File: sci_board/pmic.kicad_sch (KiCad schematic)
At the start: 21 parts, among them J1 Conn_01x03_Pin Vertical, U1 STM32L496VGTx

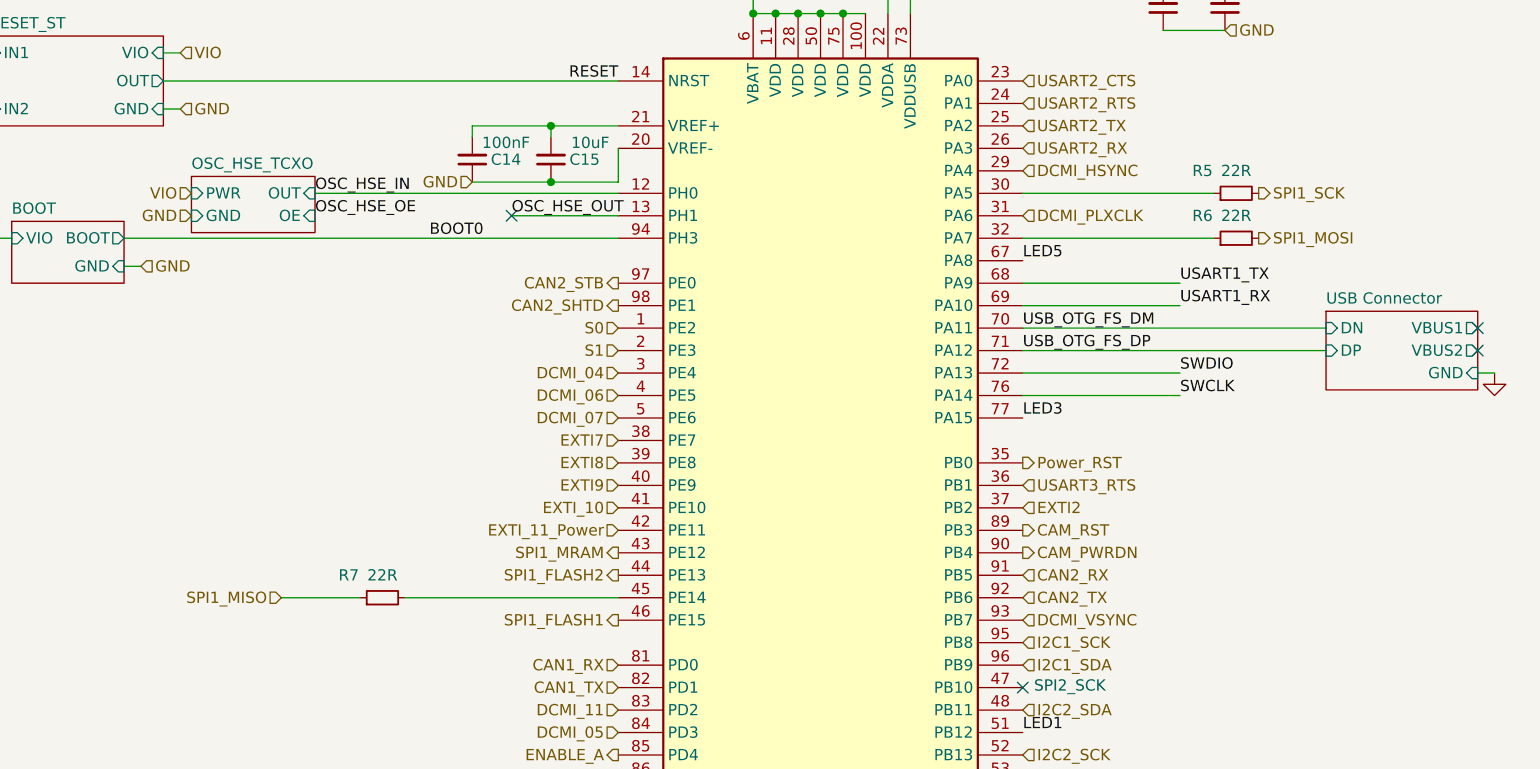
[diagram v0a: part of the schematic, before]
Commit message: SCI AVI and EPS are now consistent
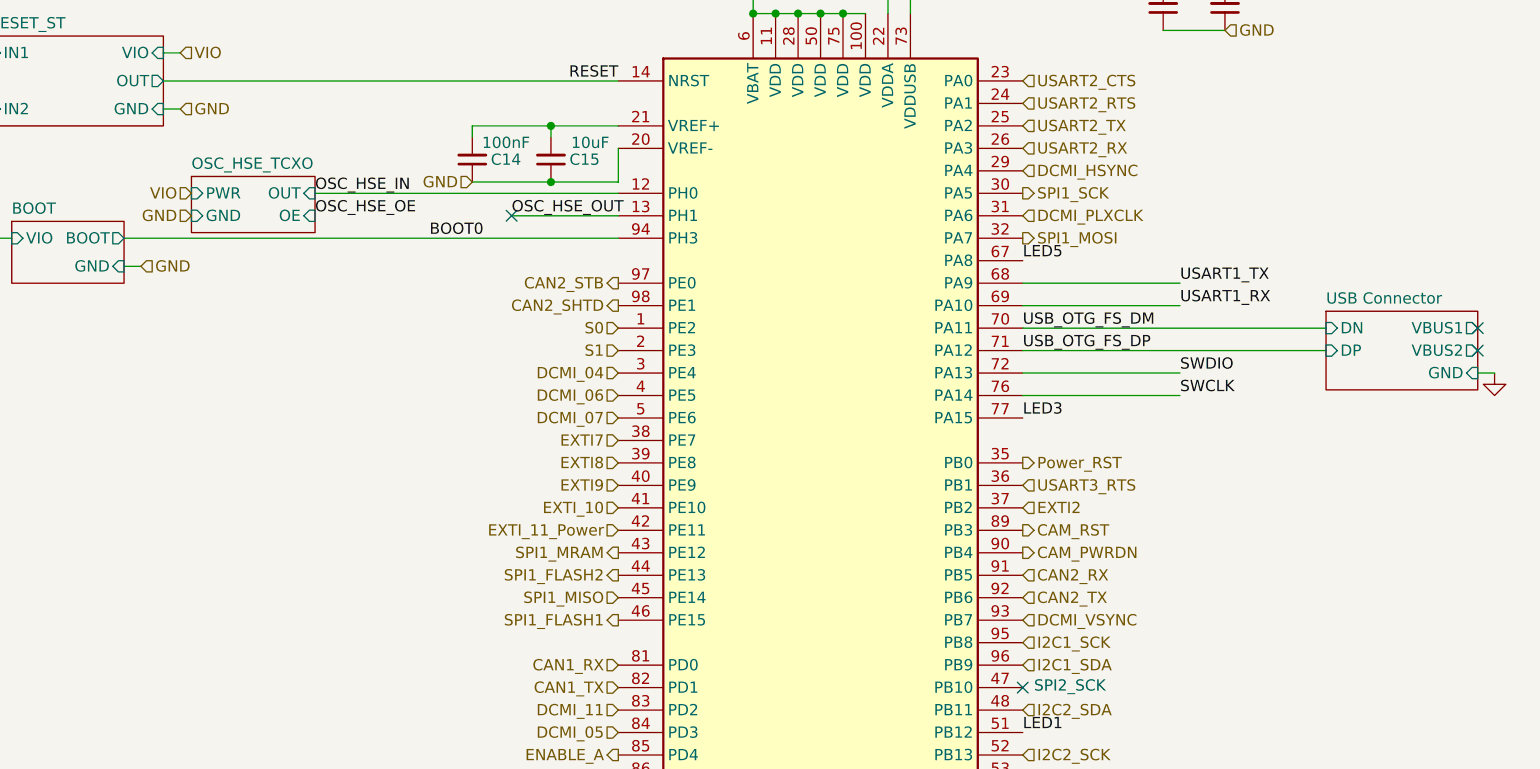
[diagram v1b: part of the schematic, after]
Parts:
- removed R5, R6, R7: 22R, Resistor_SMD:R_0402_1005Metric_Pad0.72x0.64mm_HandSolder, symbol Device:R_Small
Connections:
- net SPI1_MISO: now also U1.45 (PE14)
- net SPI1_MOSI: now also U1.32 (PA7)
- net SPI1_SCK: now also U1.30 (PA5)

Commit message: bom for SCI
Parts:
- C1, C10, C11, C13, C15, C2: MANUFACTURER Murata -> (none); Manufacturer (none) -> Murata; PARTREV GRM188R61E106KA73D -> (none); Part Number (none) -> GRM188R61E106KA73D
- C12, C14, C3, C4, C5, C6, C7, C8, C9: MANUFACTURER Murata -> (none); Manufacturer (none) -> Murata; PARTREV GRM155R61E104KA87D -> (none); Part Number (none) -> GRM155R61E104KA87D
- FB1: MANUFACTURER Murata -> (none); Manufacturer (none) -> Murata; PARTREV BLM18PG121SN1D -> (none); Part Number (none) -> BLM18PG121SN1D
- J1: MANUFACTURER generic -> (none); PARTREV generic -> (none)
- U1: MANUFACTURER STM -> (none); Manufacturer (none) -> STM; PARTREV STM32L496VGT6 -> (none); Part Number (none) -> STM32L496VGT6

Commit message: EPS AVI SCI SCIwoSwitches RF AUX all updated to use RNs. BOMs completed
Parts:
- J1: Manufacturer (none) -> generic; Part Number (none) -> vertical
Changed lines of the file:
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@@
+			)
+		)
+		(property "Manufacturer" "generic"
+			(at 248.92 100.965 0)
+			(effects
+				(font
+					(size 1.27 1.27)
+				)
+				(hide yes)
+			)
+		)
+		(property "Part Number" "vertical"
+			(at 248.92 100.965 0)
+			(effects
+				(font
+					(size 1.27 1.27)
+				)
+				(hide yes)
 			)
 		)

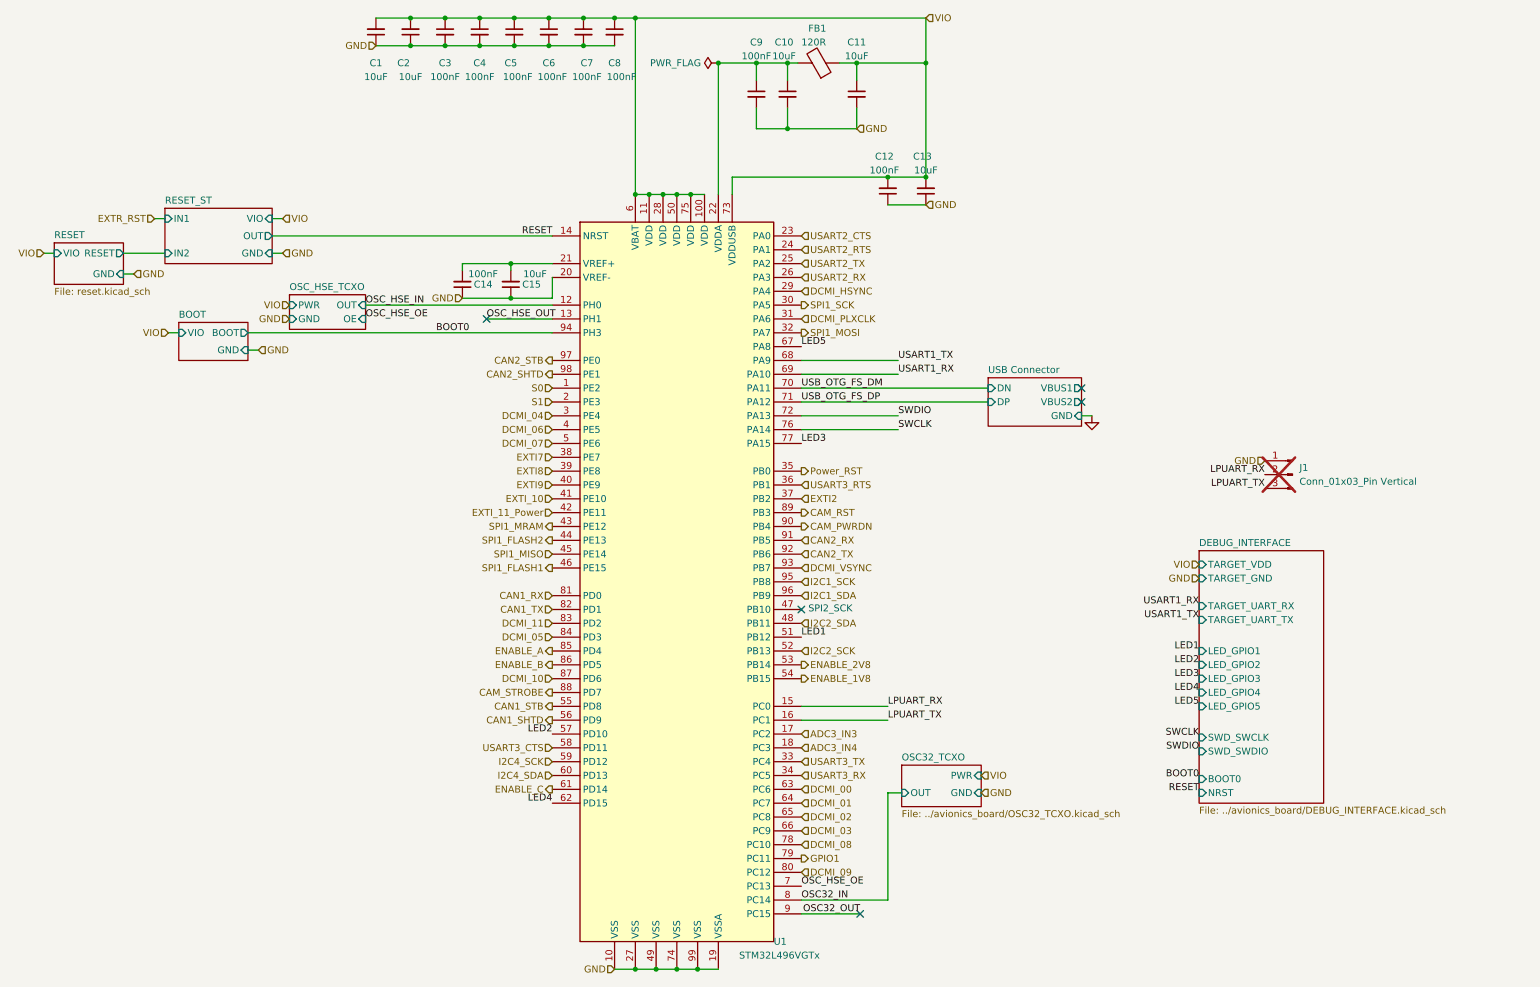
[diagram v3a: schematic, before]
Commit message: sorting out pullups on resets and attention. replace reset with RN where possible. Introduce CN to save some parts
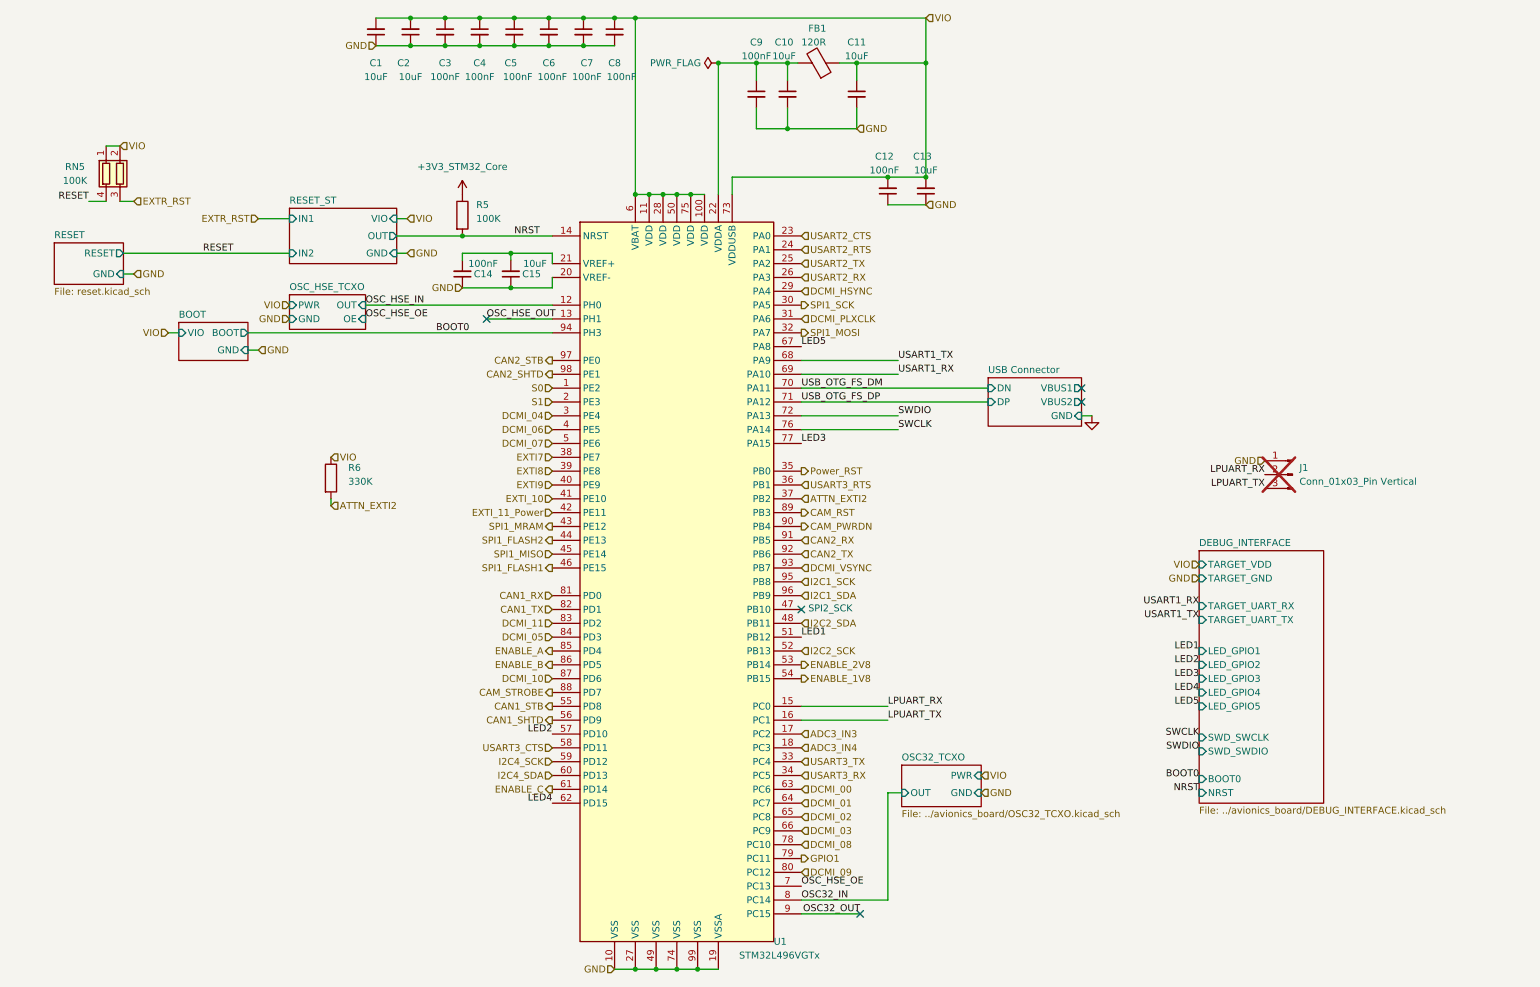
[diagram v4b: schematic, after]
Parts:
- added R5: 100K, Resistor_SMD:R_0402_1005Metric_Pad0.72x0.64mm_HandSolder, symbol Device:R
- added R6: 330K, Resistor_SMD:R_0402_1005Metric_Pad0.72x0.64mm_HandSolder, symbol Device:R
- added RN5: 100K, Resistor_SMD:R_Array_Convex_2x0402, symbol Device:R_Pack02
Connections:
- net EXTR_RST: now also RN5.3 (R2.2)
- net RESET: now also RN5.4 (R1.2); no longer U1.14 (NRST)
- net VIO: now also R6.1, RN5.1 (R1.1), RN5.2 (R2.1)
- net EXTI2 renamed ATTN_EXTI2
- net ATTN_EXTI2: now also R6.2
- new net +3V3_STM32_Core: R5.1
- new net NRST: R5.2, U1.14 (NRST)
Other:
- sheet RESET ports: added none; removed VIO
- moved on the sheet: C14, C15

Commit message: cleanup pullups for reset and schmitt trigger for reset; select available thermal NTCs for avi board and use chip for voltage dividers
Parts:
- RN5: footprint Resistor_SMD:R_Array_Convex_2x0402 -> Common:R_Array_Convex_2x0402_widepads
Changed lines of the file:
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@@
 			)
 		)
-		(property "Footprint" "Resistor_SMD:R_Array_Convex_2x0402"
+		(property "Footprint" "Common:R_Array_Convex_2x0402_widepads"
 			(at 38.1 45.72 90)
 			(effects

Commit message: checked BOM for sci wo switches
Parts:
- removed R6: 330K, Resistor_SMD:R_0402_1005Metric_Pad0.72x0.64mm_HandSolder, symbol Device:R
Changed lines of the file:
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@@
 	(wire
 		(pts
-			(xy 72.39 106.68) (xy 72.39 105.41)
-		)
-		(stroke
-			(width 0)
-			(type default)
-		)
-	)
-	(wire
-		(pts
 			(xy 174.625 51.435) (xy 181.61 51.435)
 		)
@@
 		)
 	)
-	(hierarchical_label "ATTN_EXTI2"
-		(shape input)
-		(at 72.39 106.68 0)
-		(effects
-			(font
-				(size 1.27 1.27)
-			)
-			(justify left)
-		)
-	)
 	(hierarchical_label "VIO"
 		(shape input)
@@
 		)
 	)
-	(hierarchical_label "VIO"
-		(shape input)
-		(at 72.39 97.79 0)
-		(effects
-			(font
-				(size 1.27 1.27)
-			)
-			(justify left)
-		)
-	)
 	(hierarchical_label "DCMI_PLXCLK"
 		(shape input)
@@
 					(unit 1)
 				)
-			)
-		)
-	)
-	(symbol
-		(lib_id "Device:R")
-		(at 72.39 101.6 0)
-		(unit 1)
-		(exclude_from_sim no)
-		(in_bom yes)
-		(on_board yes)
-		(dnp no)
-		(property "Reference" "R6"
-			(at 75.565 99.695 0)
-			(effects
-				(font
-					(size 1.27 1.27)
-				)
-				(justify left)
-			)
-		)
-		(property "Value" "330K"
-			(at 75.565 102.235 0)
-			(effects
-				(font
-					(size 1.27 1.27)
-				)
-				(justify left)
-			)
-		)
-		(property "Footprint" "Resistor_SMD:R_0402_1005Metric_Pad0.72x0.64mm_HandSolder"
-			(at 70.612 101.6 90)
-			(effects
-				(font
-					(size 1.27 1.27)
-				)
-				(hide yes)
-			)
-		)
-		(property "Datasheet" "https://www.yageo.com/upload/media/product/products/datasheet/rchip/PYu-RC_Group_51_RoHS_L_12.pdf"
-			(at 72.39 101.6 0)
-			(effects
-				(font
-					(size 1.27 1.27)
-				)
-				(hide yes)
-			)
-		)
-		(property "Description" "Resistor"
-			(at 72.39 101.6 0)
-			(effects
-				(font
-					(size 1.27 1.27)
-				)
-				(hide yes)
-			)
-		)
-		(property "Note" "generic pullup/down"
-			(at 72.39 101.6 0)
-			(effects
-				(font
-					(size 1.27 1.27)
-				)
-				(hide yes)
-			)
-		)
-		(property "Tolerance" "1"
-			(at 72.39 101.6 0)
-			(effects
-				(font
-					(size 1.27 1.27)
-				)
-				(hide yes)
-			)
-		)
-		(property "Manufacturer" "YAGEO"
-			(at 72.39 101.6 0)
-			(effects
-				(font
-					(size 1.27 1.27)
-				)
-				(hide yes)
-			)
-		)
-		(property "Part Number" "RC0402FR-13330K"
-			(at 72.39 101.6 0)
-			(effects
-				(font
-					(size 1.27 1.27)
-				)
-				(hide yes)
-			)
-		)
-		(pin "2"
-		)
-		(pin "1"
-		)
-		(instances
-			(project "sci_board"
-				(path "/b4b2c88d-f6cd-4e60-862d-e21f68728580/840799ac-4fe6-4a8e-96a2-299affeec8e4"
-					(reference "R6")
-					(unit 1)
-				)

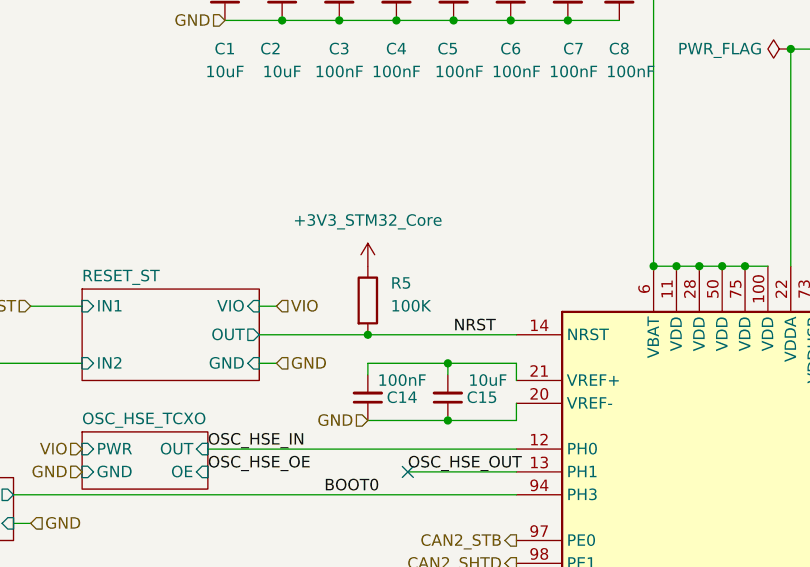
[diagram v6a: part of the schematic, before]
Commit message: EPS needs flash to self update with bootloader
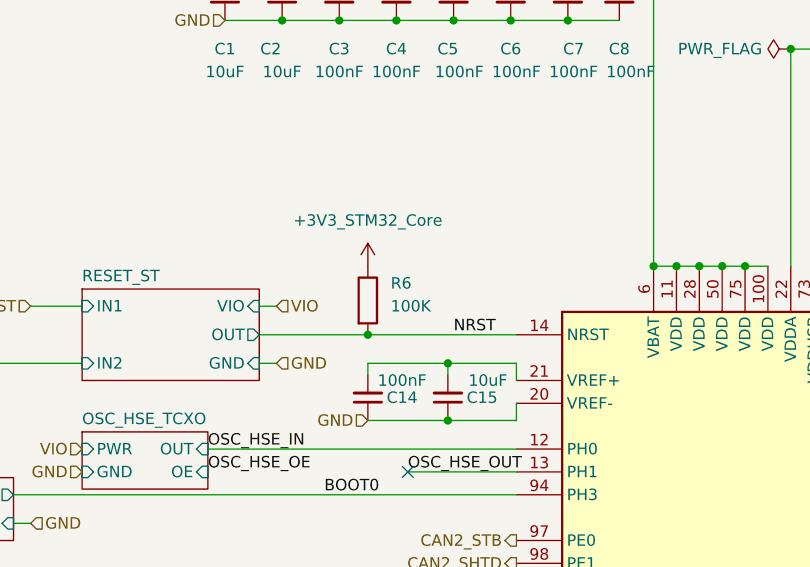
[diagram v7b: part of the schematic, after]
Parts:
- renumbered R5 to R6
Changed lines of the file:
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@@
 		(on_board yes)
 		(dnp no)
-		(property "Reference" "R5"
+		(property "Reference" "R6"
 			(at 99.06 51.435 0)
 			(effects
@@
 			(project "sci_board"
 				(path "/b4b2c88d-f6cd-4e60-862d-e21f68728580/840799ac-4fe6-4a8e-96a2-299affeec8e4"
-					(reference "R5")
+					(reference "R6")
 					(unit 1)
 				)

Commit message: move SPI CS pullups to outer schema to combine multiple with RNs
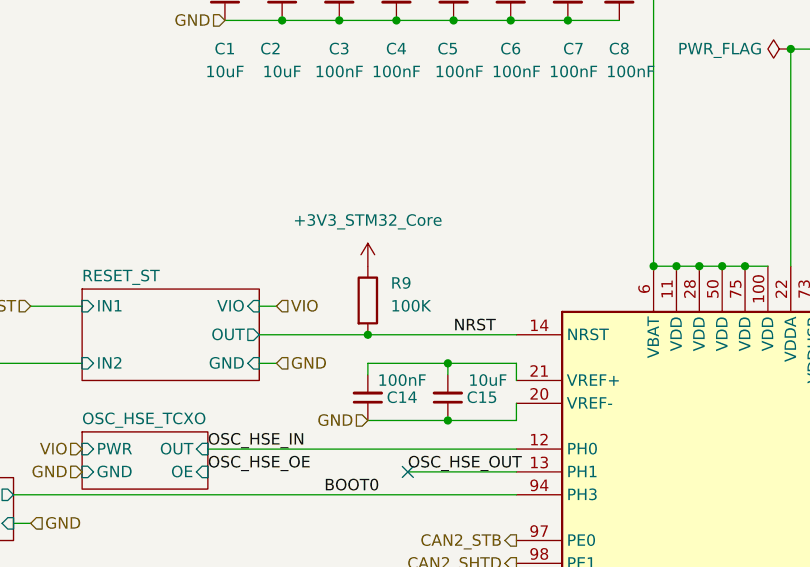
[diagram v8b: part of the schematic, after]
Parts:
- renumbered R6 to R9
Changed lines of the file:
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@@
 		(on_board yes)
 		(dnp no)
-		(property "Reference" "R6"
+		(property "Reference" "R9"
 			(at 99.06 51.435 0)
 			(effects
@@
 			(project "sci_board"
 				(path "/b4b2c88d-f6cd-4e60-862d-e21f68728580/840799ac-4fe6-4a8e-96a2-299affeec8e4"
-					(reference "R6")
+					(reference "R9")
 					(unit 1)
 				)
